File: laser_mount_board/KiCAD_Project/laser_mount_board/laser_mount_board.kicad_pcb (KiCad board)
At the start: 2 copper layers, 38.1 x 33 mm, 4 parts, among them J1 Board to Board, U1 LaserDiode

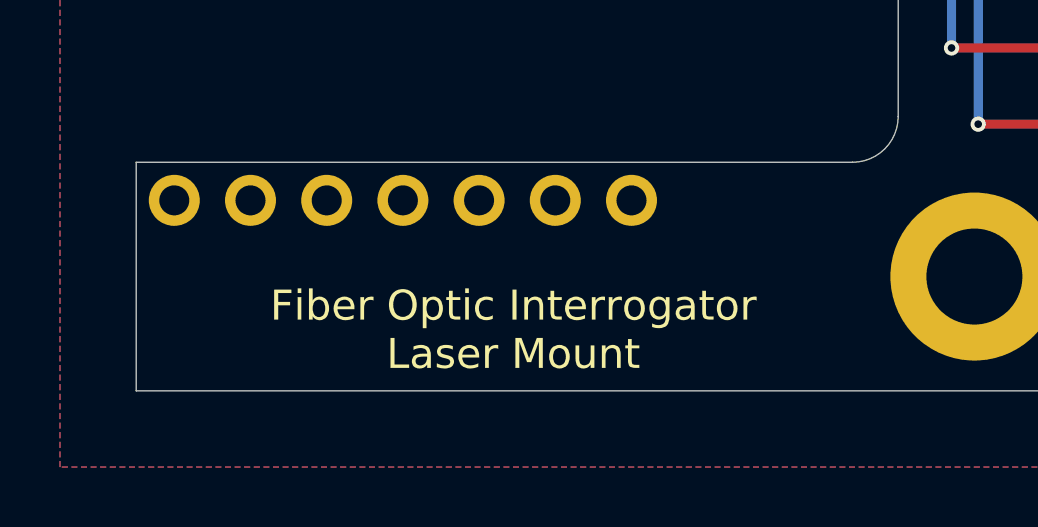
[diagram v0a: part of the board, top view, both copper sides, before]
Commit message: Update revision silkscreen text
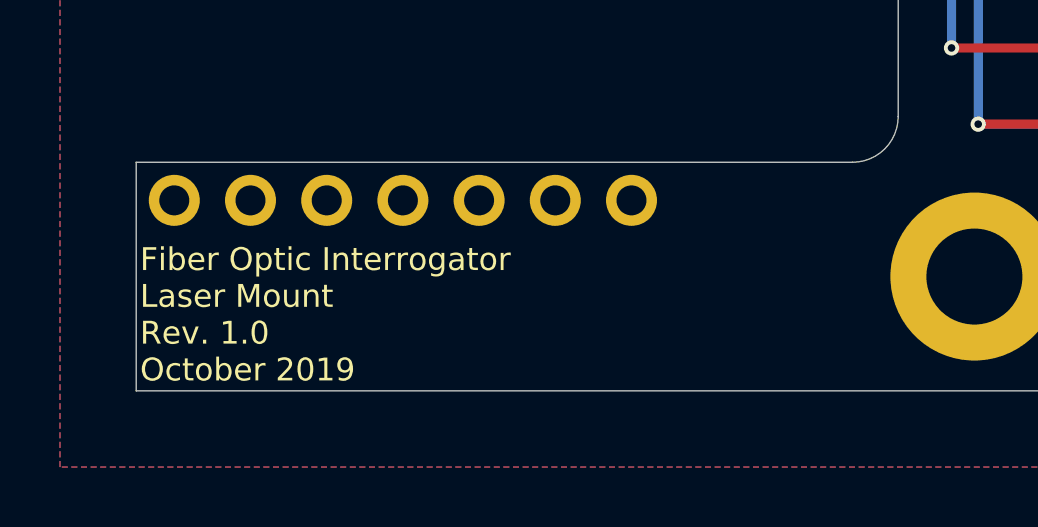
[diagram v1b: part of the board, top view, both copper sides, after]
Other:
- board text added: "Fiber Optic Interrogator Laser Mount Rev. 1.0 October 2019"
- board text removed: "Fiber Optic Interrogator Laser Mount"
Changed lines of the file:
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@@
     (effects (font (size 0.762 0.762) (thickness 0.15)) (justify mirror))
   )
-  (gr_text "Fiber Optic Interrogator\nLaser Mount" (at 130.429 116.078) (layer F.SilkS)
-    (effects (font (size 1 1) (thickness 0.15)))
+  (gr_text "Fiber Optic Interrogator\nLaser Mount\nRev. 1.0\nOctober 2019" (at 117.983 115.57) (layer F.SilkS)
+    (effects (font (size 0.762 0.762) (thickness 0.15)) (justify left))
   )
   (gr_line (start 117.856002 85.090002) (end 155.956 85.090002) (layer Edge.Cuts) (width 0.0254))

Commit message: Laser mount board ready for review.
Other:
- board text added: "OFSI Rev. 04 Laser Mount Board October 2019"
- board text removed: "Fiber Optic Interrogator Laser Mount Rev. 1.0 October 2019"
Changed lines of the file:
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@@
   )
   (setup
-    (last_trace_width 0.508)
+    (last_trace_width 0.1524)
     (user_trace_width 0.1524)
     (user_trace_width 0.254)
@@
     (aux_axis_origin 117.856002 85.090002)
     (grid_origin 117.856 85.09)
-    (visible_elements FFFFFF7F)
+    (visible_elements 7FFFFFFF)
     (pcbplotparams
       (layerselection 0x010fc_ffffffff)
@@
       (outputformat 1)
       (mirror false)
-      (drillshape 1)
+      (drillshape 0)
       (scaleselection 1)
-      (outputdirectory ""))
+      (outputdirectory "../../Production/GERBERS/"))
   )
   (net 0 "")
@@
     (effects (font (size 0.762 0.762) (thickness 0.15)) (justify mirror))
   )
-  (gr_text "Fiber Optic Interrogator\nLaser Mount\nRev. 1.0\nOctober 2019" (at 117.983 115.57) (layer F.SilkS)
+  (gr_text "OFSI Rev. 04\nLaser Mount Board\nOctober 2019" (at 117.983 115.57) (layer F.SilkS)
     (effects (font (size 0.762 0.762) (thickness 0.15)) (justify left))
   )

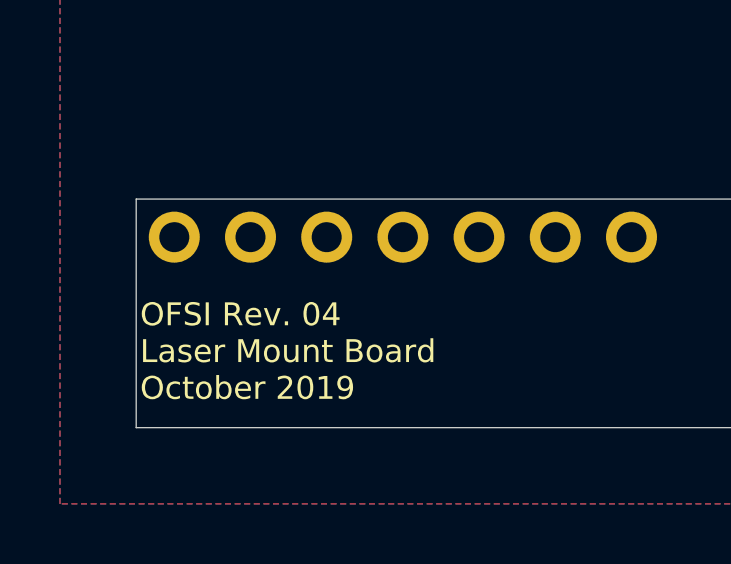
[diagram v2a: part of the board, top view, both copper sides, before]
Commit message: Change laser mount to OFMI
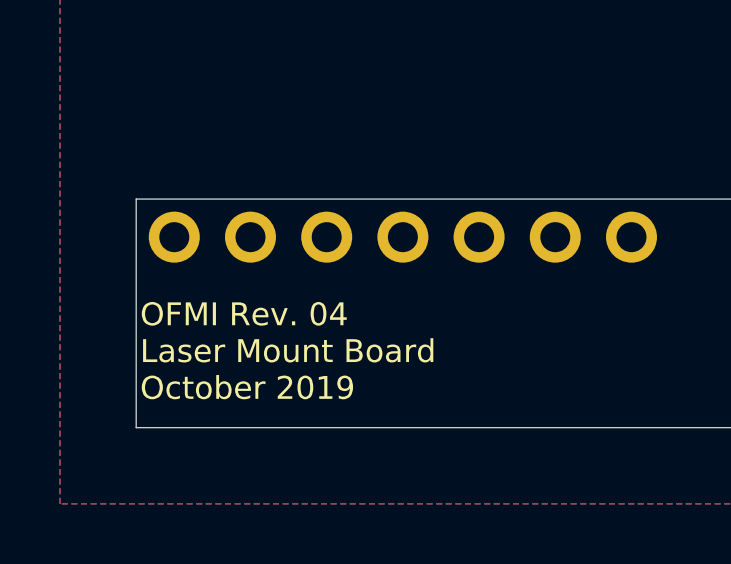
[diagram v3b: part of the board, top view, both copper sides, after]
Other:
- board text added: "OFMI Rev. 04 Laser Mount Board October 2019"
- board text removed: "OFSI Rev. 04 Laser Mount Board October 2019"
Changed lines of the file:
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@@
     (effects (font (size 0.762 0.762) (thickness 0.15)) (justify mirror))
   )
-  (gr_text "OFSI Rev. 04\nLaser Mount Board\nOctober 2019" (at 117.983 115.57) (layer F.SilkS)
+  (gr_text "OFMI Rev. 04\nLaser Mount Board\nOctober 2019" (at 117.983 115.57) (layer F.SilkS)
     (effects (font (size 0.762 0.762) (thickness 0.15)) (justify left))
   )

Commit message: Bump revisions to 4.1
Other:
- board text added: "LG 3-0000047"
- board text added: "OFMI Rev. 4.1 Laser Mount Board September 2020"
- board text removed: "LG 3-0000013"
- board text removed: "OFMI Rev. 04 Laser Mount Board October 2019"
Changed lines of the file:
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@@
-(kicad_pcb (version 20171130) (host pcbnew "(5.1.2)-1")
+(kicad_pcb (version 20171130) (host pcbnew "(5.1.5)-3")
   (general
     (thickness 1.6)
@@
     (effects (font (size 0.762 0.762) (thickness 0.15875)) (justify left mirror))
   )
-  (gr_text "LG 3-0000013" (at 122.301 117.475) (layer B.SilkS)
+  (gr_text "LG 3-0000047" (at 122.301 117.475) (layer B.SilkS)
     (effects (font (size 0.762 0.762) (thickness 0.15)) (justify mirror))
   )
-  (gr_text "OFMI Rev. 04\nLaser Mount Board\nOctober 2019" (at 117.983 115.57) (layer F.SilkS)
+  (gr_text "OFMI Rev. 4.1\nLaser Mount Board\nSeptember 2020" (at 117.983 115.57) (layer F.SilkS)
     (effects (font (size 0.762 0.762) (thickness 0.15)) (justify left))
   )
@@
   (gr_line (start 155.956 118.11) (end 117.856002 118.11) (layer Edge.Cuts) (width 0.0254))
   (via (at 145.923 109.22) (size 0.508) (drill 0.254) (layers F.Cu B.Cu) (net 1))
-  (segment (start 145.923 109.22) (end 151.892 109.22) (width 0.3048) (layer F.Cu) (net 1))
-  (segment (start 119.975999 90.590001) (end 119.126 91.44) (width 0.3048) (layer B.Cu) (net 1))
+  (segment (start 145.923 109.22) (end 151.892 109.22) (width 0.3048) (layer F.Cu) (net 1) (status 20))
+  (segment (start 119.975999 90.590001) (end 119.126 91.44) (width 0.3048) (layer B.Cu) (net 1) (status 20))
   (segment (start 145.923 109.22) (end 145.923 93.36998) (width 0.3048) (layer B.Cu) (net 1))
   (segment (start 145.923 93.36998) (end 144.42481 91.87179) (width 0.3048) (layer B.Cu) (net 1))
@@
   (segment (start 140.004581 89.827989) (end 120.738011 89.827989) (width 0.3048) (layer B.Cu) (net 1))
   (segment (start 120.738011 89.827989) (end 119.975999 90.590001) (width 0.3048) (layer B.Cu) (net 1))
-  (segment (start 145.034 106.68) (end 151.892 106.68) (width 0.3048) (layer F.Cu) (net 2))
+  (segment (start 145.034 106.68) (end 151.892 106.68) (width 0.3048) (layer F.Cu) (net 2) (status 20))
   (via (at 145.034 106.68) (size 0.508) (drill 0.254) (layers F.Cu B.Cu) (net 2))
   (segment (start 145.034 93.127571) (end 145.034 106.68) (width 0.3048) (layer B.Cu) (net 2))
@@
   (segment (start 141.859 92.329) (end 144.235428 92.329) (width 0.3048) (layer B.Cu) (net 2))
   (segment (start 139.815199 90.285199) (end 141.859 92.329) (width 0.3048) (layer B.Cu) (net 2))
-  (segment (start 121.666 91.44) (end 122.820801 90.285199) (width 0.3048) (layer B.Cu) (net 2))
+  (segment (start 121.666 91.44) (end 122.820801 90.285199) (width 0.3048) (layer B.Cu) (net 2) (status 10))
   (segment (start 122.820801 90.285199) (end 139.815199 90.285199) (width 0.3048) (layer B.Cu) (net 2))
   (via (at 144.297403 93.218) (size 0.508) (drill 0.254) (layers F.Cu B.Cu) (net 3))
   (segment (start 144.297403 93.051377) (end 144.297403 93.218) (width 0.3048) (layer F.Cu) (net 3))
   (segment (start 141.531225 90.285199) (end 144.297403 93.051377) (width 0.3048) (layer F.Cu) (net 3))
-  (segment (start 131.826 91.44) (end 132.980801 90.285199) (width 0.3048) (layer F.Cu) (net 3))
+  (segment (start 131.826 91.44) (end 132.980801 90.285199) (width 0.3048) (layer F.Cu) (net 3) (status 10))
   (segment (start 132.980801 90.285199) (end 141.531225 90.285199) (width 0.3048) (layer F.Cu) (net 3))
   (via (at 144.399 104.14) (size 0.508) (drill 0.254) (layers F.Cu B.Cu) (net 3))
   (segment (start 144.297403 93.218) (end 144.297403 104.038403) (width 0.3048) (layer B.Cu) (net 3))
   (segment (start 144.297403 104.038403) (end 144.399 104.14) (width 0.3048) (layer B.Cu) (net 3))
-  (segment (start 144.399 104.14) (end 151.892 104.14) (width 0.3048) (layer F.Cu) (net 3))
+  (segment (start 144.399 104.14) (end 151.892 104.14) (width 0.3048) (layer F.Cu) (net 3) (status 20))
   (via (at 143.637 93.218) (size 0.508) (drill 0.254) (layers F.Cu B.Cu) (net 4))
-  (segment (start 134.366 91.44) (end 141.859 91.44) (width 0.3048) (layer F.Cu) (net 4))
+  (segment (start 134.366 91.44) (end 141.859 91.44) (width 0.3048) (layer F.Cu) (net 4) (status 10))
   (segment (start 141.859 91.44) (end 143.637 93.218) (width 0.3048) (layer F.Cu) (net 4))
   (via (at 143.6751 101.6) (size 0.508) (drill 0.254) (layers F.Cu B.Cu) (net 4))
   (segment (start 143.637 93.218) (end 143.637 101.5619) (width 0.3048) (layer B.Cu) (net 4))
   (segment (start 143.637 101.5619) (end 143.6751 101.6) (width 0.3048) (layer B.Cu) (net 4))
-  (segment (start 143.6751 101.6) (end 151.892 101.6) (width 0.3048) (layer F.Cu) (net 4))
+  (segment (start 143.6751 101.6) (end 151.892 101.6) (width 0.3048) (layer F.Cu) (net 4) (status 20))
   (segment (start 130.681695 85.795199) (end 151.200199 85.795199) (width 0.3048) (layer B.Cu) (net 5))
-  (segment (start 152.741999 98.210001) (end 151.892 99.06) (width 0.3048) (layer B.Cu) (net 5))
+  (segment (start 152.741999 98.210001) (end 151.892 99.06) (width 0.3048) (layer B.Cu) (net 5) (status 20))
   (segment (start 153.046801 97.905199) (end 152.741999 98.210001) (width 0.3048) (layer B.Cu) (net 5))
   (segment (start 153.046801 87.641801) (end 153.046801 97.905199) (width 0.3048) (layer B.Cu) (net 5))
@@
   (via (at 130.681695 85.795199) (size 0.508) (drill 0.254) (layers F.Cu B.Cu) (net 5))
   (segment (start 129.850801 85.795199) (end 130.681695 85.795199) (width 0.3048) (layer F.Cu) (net 5))
-  (segment (start 124.206 91.44) (end 129.850801 85.795199) (width 0.3048) (layer F.Cu) (net 5))
-  (segment (start 127.576894 91.44) (end 133.221695 85.795199) (width 0.3048) (layer F.Cu) (net 6))
+  (segment (start 124.206 91.44) (end 129.850801 85.795199) (width 0.3048) (layer F.Cu) (net 5) (status 10))
+  (segment (start 127.576894 91.44) (end 133.221695 85.795199) (width 0.3048) (layer F.Cu) (net 6) (status 10))
   (segment (start 133.221695 85.795199) (end 151.035841 85.795199) (width 0.3048) (layer F.Cu) (net 6))
-  (segment (start 126.746 91.44) (end 127.576894 91.44) (width 0.3048) (layer F.Cu) (net 6))
+  (segment (start 126.746 91.44) (end 127.576894 91.44) (width 0.3048) (layer F.Cu) (net 6) (status 30))
   (via (at 154.559 86.487) (size 0.508) (drill 0.254) (layers F.Cu B.Cu) (net 6))
   (segment (start 151.035841 85.795199) (end 153.867199 85.795199) (width 0.3048) (layer F.Cu) (net 6))
@@
   (segment (start 154.559 94.488) (end 154.559 95.631) (width 0.3048) (layer B.Cu) (net 6))
   (segment (start 154.559 86.487) (end 154.559 94.488) (width 0.3048) (layer B.Cu) (net 6))
-  (segment (start 153.67 96.52) (end 151.892 96.52) (width 0.3048) (layer F.Cu) (net 6))
+  (segment (start 153.67 96.52) (end 151.892 96.52) (width 0.3048) (layer F.Cu) (net 6) (status 20))
   (segment (start 145.034 93.141382) (end 145.034 93.218) (width 0.3048) (layer F.Cu) (net 7))
   (segment (start 141.720608 89.82799) (end 145.034 93.141382) (width 0.3048) (layer F.Cu) (net 7))
-  (segment (start 129.286 91.44) (end 130.89801 89.82799) (width 0.3048) (layer F.Cu) (net 7))
+  (segment (start 129.286 91.44) (end 130.89801 89.82799) (width 0.3048) (layer F.Cu) (net 7) (status 10))
   (segment (start 130.89801 89.82799) (end 141.720608 89.82799) (width 0.3048) (layer F.Cu) (net 7))
-  (segment (start 150.689919 93.98) (end 151.892 93.98) (width 0.3048) (layer F.Cu) (net 7))
+  (segment (start 150.689919 93.98) (end 151.892 93.98) (width 0.3048) (layer F.Cu) (net 7) (status 20))
   (segment (start 145.43679 93.98) (end 150.689919 93.98) (width 0.3048) (layer F.Cu) (net 7))
   (segment (start 145.034 93.57721) (end 145.43679 93.98) (width 0.3048) (layer F.Cu) (net 7))

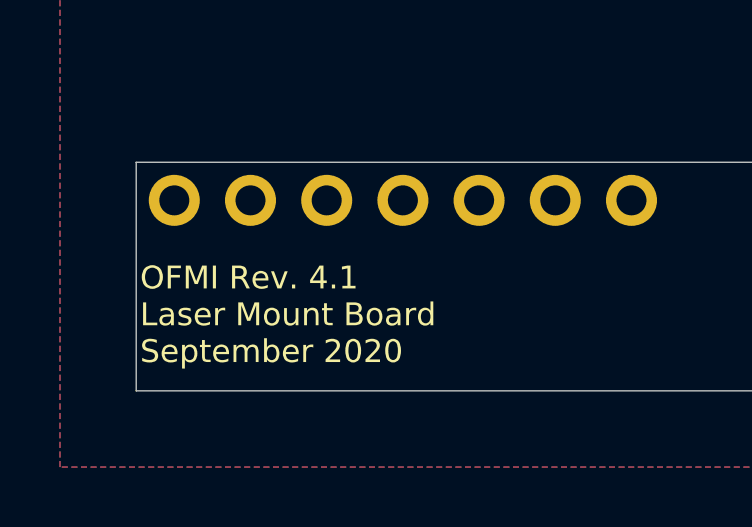
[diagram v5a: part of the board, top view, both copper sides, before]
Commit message: Update laser mount board to Rev 4.2. Closes #35
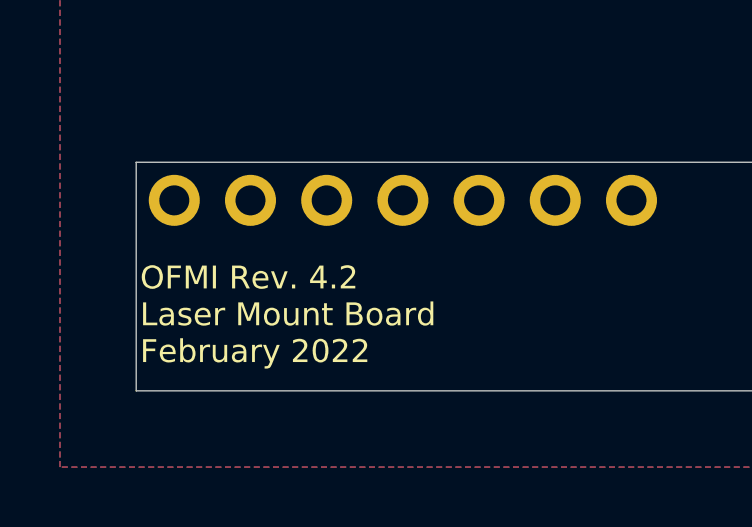
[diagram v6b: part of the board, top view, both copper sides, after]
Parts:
- added PCB1: barepcb, misc:barepcb, F.Cu at (152.3, 120.9)
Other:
- rule pad_to_mask_clearance: 0.0508 -> 0
- board text added: "3-0000122"
- board text added: "OFMI Rev. 4.2 Laser Mount Board February 2022"
- board text removed: "LG 3-0000047"
- board text removed: "OFMI Rev. 4.1 Laser Mount Board September 2020"
